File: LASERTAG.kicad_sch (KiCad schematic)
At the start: 29 parts, among them J1 Conn_01x02_Pin, J2 USB_C_Receptacle_USB2.0_14P, J3 Conn_01x02_Pin, SW1 SW_Push, SW2 SW_Push, U1 ATMEGA328-AU, U2 ESP32-S2-SOLO, U3 TPS613221ADBVR, U4 TPS613221ADBVR, U5 AP7366-33W5-7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

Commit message: feedback changes
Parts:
- added C11, C12: 10uF, symbol Device:C
- added C13, C14: 2.2uF, symbol Device:C
- added D2, D3: D_Schottky, symbol Device:D_Schottky
- added SW3, SW4: SW_SPST, symbol Switch:SW_SPST
- C5, C6: value 22uF -> 10uF
- C7: value .1uF -> 1uF
- L1, L2: value 4.7uH -> 2.2uH
- renumbered 5.1k to 5.1k1
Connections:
- net +3.3V: now also C11.1, D3.1 (K); no longer U4.4 (VOUT)
- net +3V3: now also U1.18 (AVCC), C12.1, D2.1 (K); no longer U3.4 (VOUT)
- net GND: now also C11.2, C12.2, C13.2, C14.2
- net at L1.1: now also C14.1, SW4.2 (B); no longer J1.1 (Pin_1)
- net at J3.1 (Pin_1): now also SW3.1 (A); no longer L2.1
- new net: D2.2 (A), U3.4 (VOUT)
- new net: J1.1 (Pin_1), SW4.1 (A)
- new net: C13.1, L2.1, SW3.2 (B)
- new net: D3.2 (A), U4.4 (VOUT)
- no-connect marks 6 -> 5
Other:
- moved on the sheet: C5, C6, J3, L1, L2, U3, U4

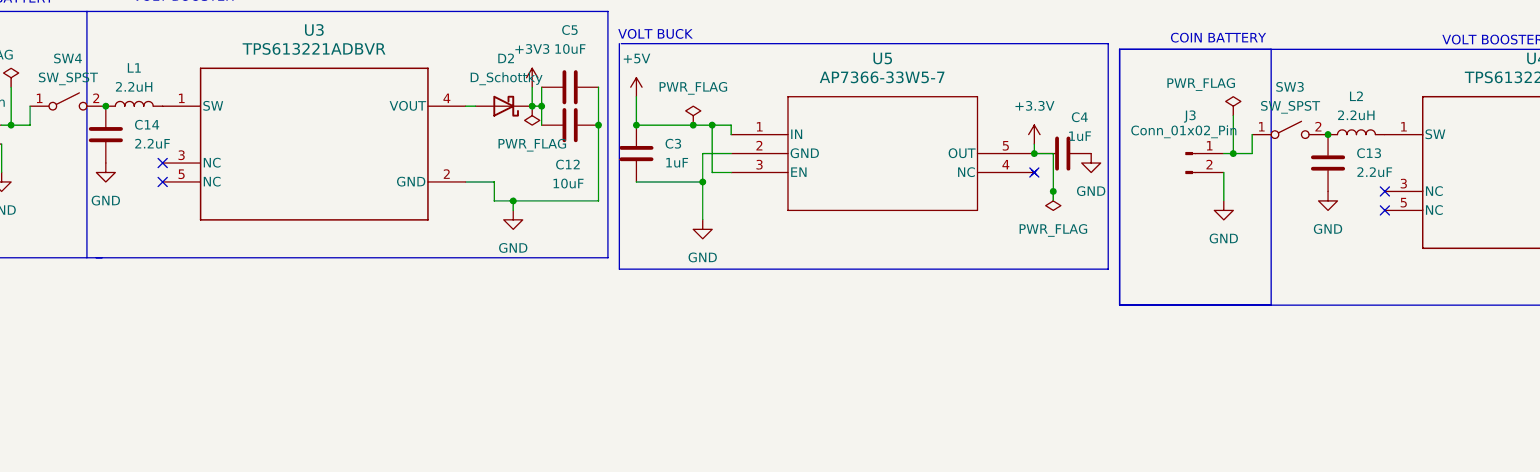
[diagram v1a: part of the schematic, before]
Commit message: temp added diff booster, assigned footprints, changes from feedback
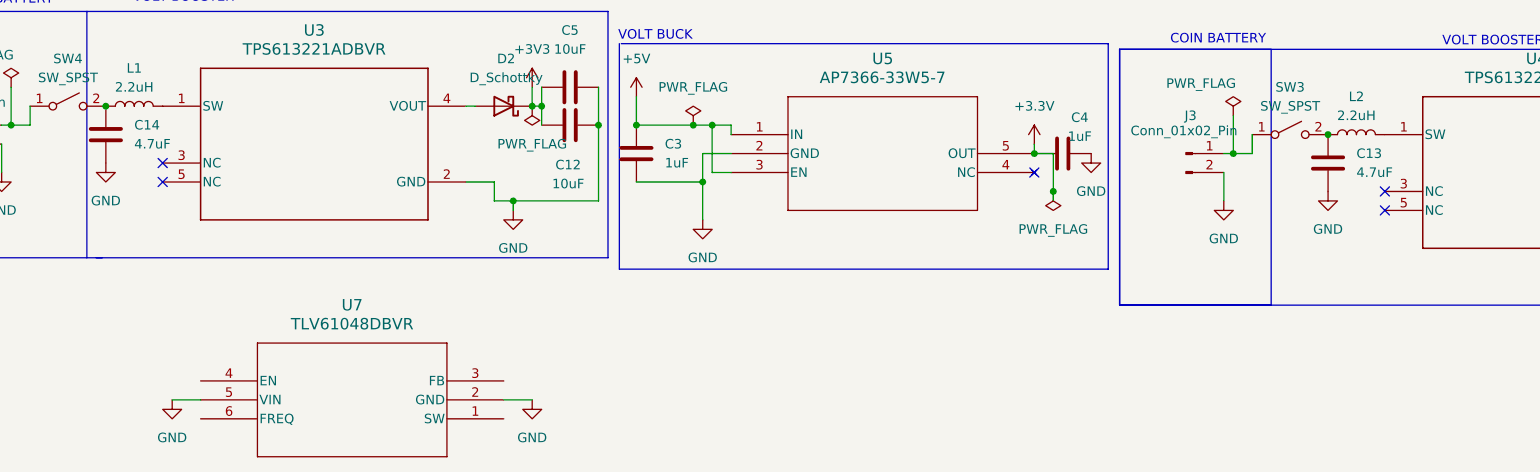
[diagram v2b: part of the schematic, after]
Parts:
- added U7: TLV61048DBVR, footprints:SOT-23-6_DBV_TEX, symbol 2024-11-02_21-57-25:TLV61048DBVR
- 5.1k1, R1, R2, R4, R5: footprint (none) -> Resistor_SMD:R_0805_2012Metric
- C1, C10, C11, C12, C2, C3, C4, C5, C6, C7, C8, C9: footprint (none) -> Capacitor_SMD:C_0805_2012Metric
- C13, C14: value 2.2uF -> 4.7uF; footprint (none) -> Capacitor_SMD:C_0805_2012Metric
- D1: footprint (none) -> LED_SMD:LED_0805_2012Metric
- D2, D3: footprint (none) -> Diode_SMD:D_3220_8050Metric
- L1, L2: footprint (none) -> Inductor_SMD:L_0805_2012Metric
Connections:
- net GND: now also U7.2 (GND), U7.5 (VIN)

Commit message: fix a lot of things i don't remember sorryy
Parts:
- removed 5.1k1: R, Resistor_SMD:R_0805_2012Metric, symbol Device:R
- removed C10: .1uF, Capacitor_SMD:C_0805_2012Metric, symbol Device:C
- removed C12, C5: 10uF, Capacitor_SMD:C_0805_2012Metric, symbol Device:C
- removed C14: 4.7uF, Capacitor_SMD:C_0805_2012Metric, symbol Device:C
- removed D1: LED, LED_SMD:LED_0805_2012Metric, symbol Device:LED
- removed D2, D3: D_Schottky, Diode_SMD:D_3220_8050Metric, symbol Device:D_Schottky
- removed J1, J3: Conn_01x02_Pin, symbol Connector:Conn_01x02_Pin
- removed J2: USB_C_Receptacle_USB2.0_14P, symbol Connector:USB_C_Receptacle_USB2.0_14P
- removed L1: 2.2uH, Inductor_SMD:L_0805_2012Metric, symbol Device:L
- removed R4: 5.1k, Resistor_SMD:R_0805_2012Metric, symbol Device:R
- removed SW1, SW2: SW_Push, symbol Switch:SW_Push
- removed SW3, SW4: SW_SPST, symbol Switch:SW_SPST
- removed U1: ATMEGA328-AU, digikey-footprints:TQFP-32_7x7mm, symbol dk_Embedded-Microcontrollers:ATMEGA328-AU
- removed U3: TPS613221ADBVR, DBV0005A_N, symbol 2024-10-19_05-20-17:TPS613221ADBVR
- removed U7: TLV61048DBVR, footprints:SOT-23-6_DBV_TEX, symbol 2024-11-02_21-57-25:TLV61048DBVR
- added B1: BAT-HLD-001, BAT_HLD_001:BATT_HLDR_LNX, symbol 2024-11-03_05-52-53:BAT-HLD-001
- added D1: D_Schottky, Diode_SMD:D_3220_8050Metric, symbol Device:D_Schottky
- added J1: USB4105-GF-A, USB4105_GF_A_2:GCT_USB4105-GF-A, symbol 2024-11-03_05-17-58:USB4105-GF-A
- added R3: 5.1k, Resistor_SMD:R_0805_2012Metric, symbol Device:R
- added SW1, SW2: B3F-1000, B3F_1000:SW_B3F-1000_OMR, symbol 2024-11-03_04-49-53:B3F-1000
- added SW4: 1825255-1, 1825255_1:SW3_1825255-1_TEC, symbol 2024-11-03_03-58-19:1825255-1
- R1: value 100 -> 5.1k
- U2: footprint PCM_Espressif:ESP32-S2-SOLO -> ESP32_S2_SOLO_N4:XCVR_ESP32-S2-SOLO-N4
- U4: footprint DBV0005A_N -> TPS613221ADBVR:DBV0005A_N
- U5: footprint SOT25-YE_DIO -> AP7366_33W5_7:SOT25-YE_DIO
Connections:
- net +3.3V: now also U4.4 (VOUT)
- net +5V: now also D1.2 (A), J1.A4-B9 (VBUS), J1.B4-A9 (VBUS); no longer U5.1 (IN)
- net D+: now also J1.A6 (DP1), J1.B6 (DP2)
- net D-: now also J1.A7 (DN1), J1.B7 (DN2)
- net GND: now also R1.2, B1.2, J1.A1-B12 (GND), J1.A8 (SBU1), J1.B1-A12 (GND), J1.B8 (SBU2), R3.1, SW1.4, SW2.1
- net at C2.2, R2.2, U2.3 (EN): now also SW2.4
- net at C13.1, L2.1: now also SW4.2
- net at C1.1, U2.27 (GPIO0): now also SW1.1
- net at R1.1: now also J1.A5 (CC1)
- new net: D1.1 (K), U5.1 (IN)
- new net: J1.B5 (CC2), R3.2
- new net: B1.1, B1.3, SW4.1
- no-connect marks 5 -> 36
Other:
- note removed: "IR TRANCIVER"
- moved on the sheet: C11, C13, C2, C3, C4, C6, C7, C8, C9, L2, R2, R5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
